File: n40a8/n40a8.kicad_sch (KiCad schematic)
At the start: 93 parts, among them J1 Conn_01x16, SW1 SW_Push, SW10 SW_Push, SW11 SW_Push, SW12 SW_Push, SW13 SW_Push, SW14 SW_Push, SW15 SW_Push, SW16 SW_Push, SW17 SW_Push, SW18 SW_Push, SW19 SW_Push, SW2 SW_Push, SW20 SW_Push, SW21 SW_Push, SW22 SW_Push, SW23 SW_Push, SW24 SW_Push, SW25 SW_Push, SW26 SW_Push, SW27 SW_Push, SW28 SW_Push, SW29 SW_Push, SW3 SW_Push, SW30 SW_Push, SW31 SW_Push, SW32 SW_Push, SW33 SW_Push, SW34 SW_Push, SW35 SW_Push, SW36 SW_Push, SW37 SW_Push, SW38 SW_Push, SW39 SW_Push, SW4 SW_Push, SW40 SW_Push, SW41 SW_Push, SW42 SW_Push, SW43 SW_RST, SW44 SW_PWR, SW5 SW_Push, SW6 SW_Push, SW7 SW_Push, SW8 SW_Push, SW9 SW_Push, U1 BLE-Micro-Pro-2, U2 TPS61221

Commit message: move Diode
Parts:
- SW38: footprint cscslib:CPG151101S11_2u_RS -> cscslib:CPG151101S11_2u
- SW39: footprint cscslib:CPG151101S11_1.25u -> cscslib:CPG151101S11_2.25u
- SW40: footprint cscslib:CPG151101S11_2.25u_RS -> cscslib:CPG151101S11_1.25u
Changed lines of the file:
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@@
 			)
 		)
-		(property "Footprint" "cscslib:CPG151101S11_1.25u"
+		(property "Footprint" "cscslib:CPG151101S11_2.25u"
 			(at 137.16 115.57 0)
 			(effects
@@
 			)
 		)
-		(property "Footprint" "cscslib:CPG151101S11_2u_RS"
+		(property "Footprint" "cscslib:CPG151101S11_2u"
 			(at 83.82 115.57 0)
 			(effects
@@
 			)
 		)
-		(property "Footprint" "cscslib:CPG151101S11_2.25u_RS"
+		(property "Footprint" "cscslib:CPG151101S11_1.25u"
 			(at 154.94 115.57 0)
 			(effects

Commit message: wired
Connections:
- net C2: no longer SW37.1
- net C3: now also SW37.1; no longer SW38.1
- net C4: now also SW38.1
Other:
- moved on the sheet: D37, D38, SW37, SW38
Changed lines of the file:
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@@
 	)
 	(junction
-		(at 71.12 128.27)
-		(diameter 0)
-		(color 0 0 0 0)
-	)
-	(junction
 		(at 185.42 87.63)
 		(diameter 0)
@@
 	)
 	(junction
-		(at 78.74 104.14)
+		(at 96.52 71.12)
 		(diameter 0)
 		(color 0 0 0 0)
 	)
 	(junction
-		(at 96.52 71.12)
+		(at 106.68 128.27)
 		(diameter 0)
 		(color 0 0 0 0)
@@
 	)
 	(junction
+		(at 88.9 128.27)
+		(diameter 0)
+		(color 0 0 0 0)
+	)
+	(junction
 		(at 167.64 71.12)
 		(diameter 0)
@@
 	)
 	(junction
+		(at 78.74 104.14)
+		(diameter 0)
+		(color 0 0 0 0)
+	)
+	(junction
 		(at 29.21 176.53)
 		(diameter 0)
@@
 	)
 	(junction
-		(at 88.9 128.27)
-		(diameter 0)
-		(color 0 0 0 0)
-	)
-	(junction
 		(at 35.56 78.74)
 		(diameter 0)
@@
 	)
 	(junction
-		(at 60.96 104.14)
+		(at 160.02 95.25)
 		(diameter 0)
 		(color 0 0 0 0)
 	)
 	(junction
-		(at 160.02 95.25)
+		(at 96.52 104.14)
 		(diameter 0)
 		(color 0 0 0 0)
@@
 	(wire
 		(pts
-			(xy 203.2 71.12) (xy 203.2 87.63)
+			(xy 106.68 128.27) (xy 142.24 128.27)
 		)
 		(stroke
@@
 	(wire
 		(pts
-			(xy 60.96 48.26) (xy 66.04 48.26)
+			(xy 203.2 71.12) (xy 203.2 87.63)
 		)
 		(stroke
@@
 	(wire
 		(pts
-			(xy 177.8 111.76) (xy 195.58 111.76)
+			(xy 60.96 48.26) (xy 66.04 48.26)
 		)
 		(stroke
@@
 	(wire
 		(pts
-			(xy 40.64 167.64) (xy 62.23 167.64)
+			(xy 177.8 111.76) (xy 195.58 111.76)
 		)
 		(stroke
@@
 	(wire
 		(pts
-			(xy 269.24 55.88) (xy 269.24 54.61)
+			(xy 40.64 167.64) (xy 62.23 167.64)
 		)
 		(stroke
@@
 	(wire
 		(pts
-			(xy 106.68 78.74) (xy 124.46 78.74)
+			(xy 269.24 55.88) (xy 269.24 54.61)
 		)
 		(stroke
@@
 	(wire
 		(pts
-			(xy 63.5 181.61) (xy 63.5 182.88)
+			(xy 106.68 78.74) (xy 124.46 78.74)
 		)
 		(stroke
@@
 	(wire
 		(pts
-			(xy 231.14 78.74) (xy 241.3 78.74)
+			(xy 63.5 181.61) (xy 63.5 182.88)
 		)
 		(stroke
@@
 	(wire
 		(pts
-			(xy 60.96 104.14) (xy 60.96 120.65)
+			(xy 231.14 78.74) (xy 241.3 78.74)
 		)
 		(stroke
@@
 	(wire
 		(pts
-			(xy 53.34 128.27) (xy 71.12 128.27)
+			(xy 53.34 128.27) (xy 88.9 128.27)
 		)
 		(stroke
@@
 	(wire
 		(pts
-			(xy 149.86 71.12) (xy 149.86 87.63)
+			(xy 78.74 104.14) (xy 78.74 120.65)
 		)
 		(stroke
@@
 	(wire
 		(pts
-			(xy 88.9 95.25) (xy 106.68 95.25)
+			(xy 149.86 71.12) (xy 149.86 87.63)
 		)
 		(stroke
@@
 	(wire
 		(pts
-			(xy 71.12 128.27) (xy 88.9 128.27)
+			(xy 88.9 95.25) (xy 106.68 95.25)
 		)
 		(stroke
@@
 	(wire
 		(pts
+			(xy 88.9 128.27) (xy 106.68 128.27)
+		)
+		(stroke
+			(width 0)
+			(type default)
+		)
+	)
+	(wire
+		(pts
 			(xy 177.8 78.74) (xy 195.58 78.74)
 		)
@@
 	(wire
 		(pts
-			(xy 88.9 128.27) (xy 142.24 128.27)
-		)
-		(stroke
-			(width 0)
-			(type default)
-		)
-	)
-	(wire
-		(pts
 			(xy 38.1 189.23) (xy 38.1 190.5)
 		)
@@
 	(wire
 		(pts
+			(xy 96.52 104.14) (xy 96.52 120.65)
+		)
+		(stroke
+			(width 0)
+			(type default)
+		)
+	)
+	(wire
+		(pts
 			(xy 60.96 50.8) (xy 66.04 50.8)
 		)
@@
 	(wire
 		(pts
-			(xy 78.74 104.14) (xy 78.74 120.65)
-		)
-		(stroke
-			(width 0)
-			(type default)
-		)
-	)
-	(wire
-		(pts
 			(xy 78.74 63.5) (xy 78.74 71.12)
 		)
@@
 	(symbol
 		(lib_id "Switch:SW_Push")
-		(at 83.82 120.65 0)
+		(at 101.6 120.65 0)
 		(unit 1)
 		(exclude_from_sim no)
@@
 		(dnp no)
 		(property "Reference" "SW38"
-			(at 83.82 113.411 0)
+			(at 101.6 113.411 0)
 			(effects
 				(font
@@
 		)
 		(property "Value" "SW_Push"
-			(at 83.82 115.7224 0)
+			(at 101.6 115.7224 0)
 			(effects
 				(font
@@
 		)
 		(property "Footprint" "cscslib:CPG151101S11_2u"
-			(at 83.82 115.57 0)
+			(at 101.6 115.57 0)
 			(effects
 				(font
@@
 		)
 		(property "Datasheet" ""
-			(at 83.82 115.57 0)
+			(at 101.6 115.57 0)
 			(effects
 				(font
@@
 		)
 		(property "Description" ""
-			(at 83.82 120.65 0)
+			(at 101.6 120.65 0)
 			(effects
 				(font
@@
 	(symbol
 		(lib_id "Switch:SW_Push")
-		(at 66.04 120.65 0)
+		(at 83.82 120.65 0)
 		(unit 1)
 		(exclude_from_sim no)
@@
 		(dnp no)
 		(property "Reference" "SW37"
-			(at 66.04 113.411 0)
+			(at 83.82 113.411 0)
 			(effects
 				(font
@@
 		)
 		(property "Value" "SW_Push"
-			(at 66.04 115.7224 0)
+			(at 83.82 115.7224 0)
 			(effects
 				(font
@@
 		)
 		(property "Footprint" "cscslib:CPG151101S11_1.25u"
-			(at 66.04 115.57 0)
+			(at 83.82 115.57 0)
 			(effects
 				(font
@@
 		)
 		(property "Datasheet" ""
-			(at 66.04 115.57 0)
+			(at 83.82 115.57 0)
 			(effects
 				(font
@@
 		)
 		(property "Description" ""
-			(at 66.04 120.65 0)
+			(at 83.82 120.65 0)
 			(effects
 				(font
@@
 	(symbol
 		(lib_id "Diode:1N4148W")
-		(at 88.9 124.46 90)
+		(at 106.68 124.46 90)
 		(unit 1)
 		(exclude_from_sim no)
@@
 		(dnp no)
 		(property "Reference" "D38"
-			(at 90.6272 123.2916 90)
+			(at 108.4072 123.2916 90)
 			(effects
 				(font
@@
 		)
 		(property "Value" "D"
-			(at 90.6272 125.603 90)
+			(at 108.4072 125.603 90)
 			(effects
 				(font
@@
 		)
 		(property "Footprint" "Diode_SMD:D_SOD-123"
-			(at 93.345 124.46 0)
+			(at 111.125 124.46 0)
 			(effects
 				(font
@@
 		)
 		(property "Datasheet" "https://www.vishay.com/docs/85748/1n4148w.pdf"
-			(at 88.9 124.46 0)
+			(at 106.68 124.46 0)
 			(effects
 				(font
@@
 		)
 		(property "Description" "75V 0.15A Fast Switching Diode, SOD-123"
-			(at 88.9 124.46 0)
+			(at 106.68 124.46 0)
 			(effects
 				(font
@@
 		)
 		(property "Sim.Device" "D"
-			(at 88.9 124.46 0)
+			(at 106.68 124.46 0)
 			(effects
 				(font
@@
 		)
 		(property "Sim.Pins" "1=K 2=A"
-			(at 88.9 124.46 0)
+			(at 106.68 124.46 0)
 			(effects
 				(font
@@
 	(symbol
 		(lib_id "Diode:1N4148W")
-		(at 71.12 124.46 90)
+		(at 88.9 124.46 90)
 		(unit 1)
 		(exclude_from_sim no)
@@
 		(dnp no)
 		(property "Reference" "D37"
-			(at 72.8472 123.2916 90)
+			(at 90.6272 123.2916 90)
 			(effects
 				(font
@@
 		)
 		(property "Value" "D"
-			(at 72.8472 125.603 90)
+			(at 90.6272 125.603 90)
 			(effects
 				(font
@@
 		)
 		(property "Footprint" "Diode_SMD:D_SOD-123"
-			(at 75.565 124.46 0)
+			(at 93.345 124.46 0)
 			(effects
 				(font
@@
 		)
 		(property "Datasheet" "https://www.vishay.com/docs/85748/1n4148w.pdf"
-			(at 71.12 124.46 0)
+			(at 88.9 124.46 0)
 			(effects
 				(font
@@
 		)
 		(property "Description" "75V 0.15A Fast Switching Diode, SOD-123"
-			(at 71.12 124.46 0)
+			(at 88.9 124.46 0)
 			(effects
 				(font
@@
 		)
 		(property "Sim.Device" "D"
-			(at 71.12 124.46 0)
+			(at 88.9 124.46 0)
 			(effects
 				(font
@@
 		)
 		(property "Sim.Pins" "1=K 2=A"
-			(at 71.12 124.46 0)
+			(at 88.9 124.46 0)
 			(effects
 				(font

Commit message: wiring complete
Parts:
- removed J1: Conn_01x16, cscslib:PinHeader_1x16_P1.27mm_Conthrough, symbol Connector_Generic:Conn_01x16
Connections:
- net C0: now also U1.14 (PB2); no longer U1.12 (PB5)
- net C1: now also U1.15 (PB3); no longer U1.11 (PB4)
- net C10: now also U1.5 (SCL); no longer U1.18 (PF6)
- net C2: now also U1.16 (PB1); no longer U1.10 (PE6)
- net C3: now also U1.17 (PF7); no longer U1.9 (PD7)
- net C4: now also U1.18 (PF6); no longer U1.8 (PC6)
- net C5: now also U1.19 (PF5); no longer U1.7 (PD4)
- net C6: now also U1.20 (PF4); no longer U1.6 (SDA)
- net C7: now also U1.8 (PC6); no longer U1.5 (SCL)
- net C8: now also U1.7 (PD4); no longer U1.20 (PF4)
- net C9: now also U1.6 (SDA); no longer U1.19 (PF5)
- net R0: now also U1.12 (PB5); no longer U1.17 (PF7)
- net R1: now also U1.11 (PB4); no longer U1.16 (PB1)
- net R2: now also U1.10 (PE6); no longer U1.15 (PB3)
- net R3: now also U1.9 (PD7); no longer U1.14 (PB2)

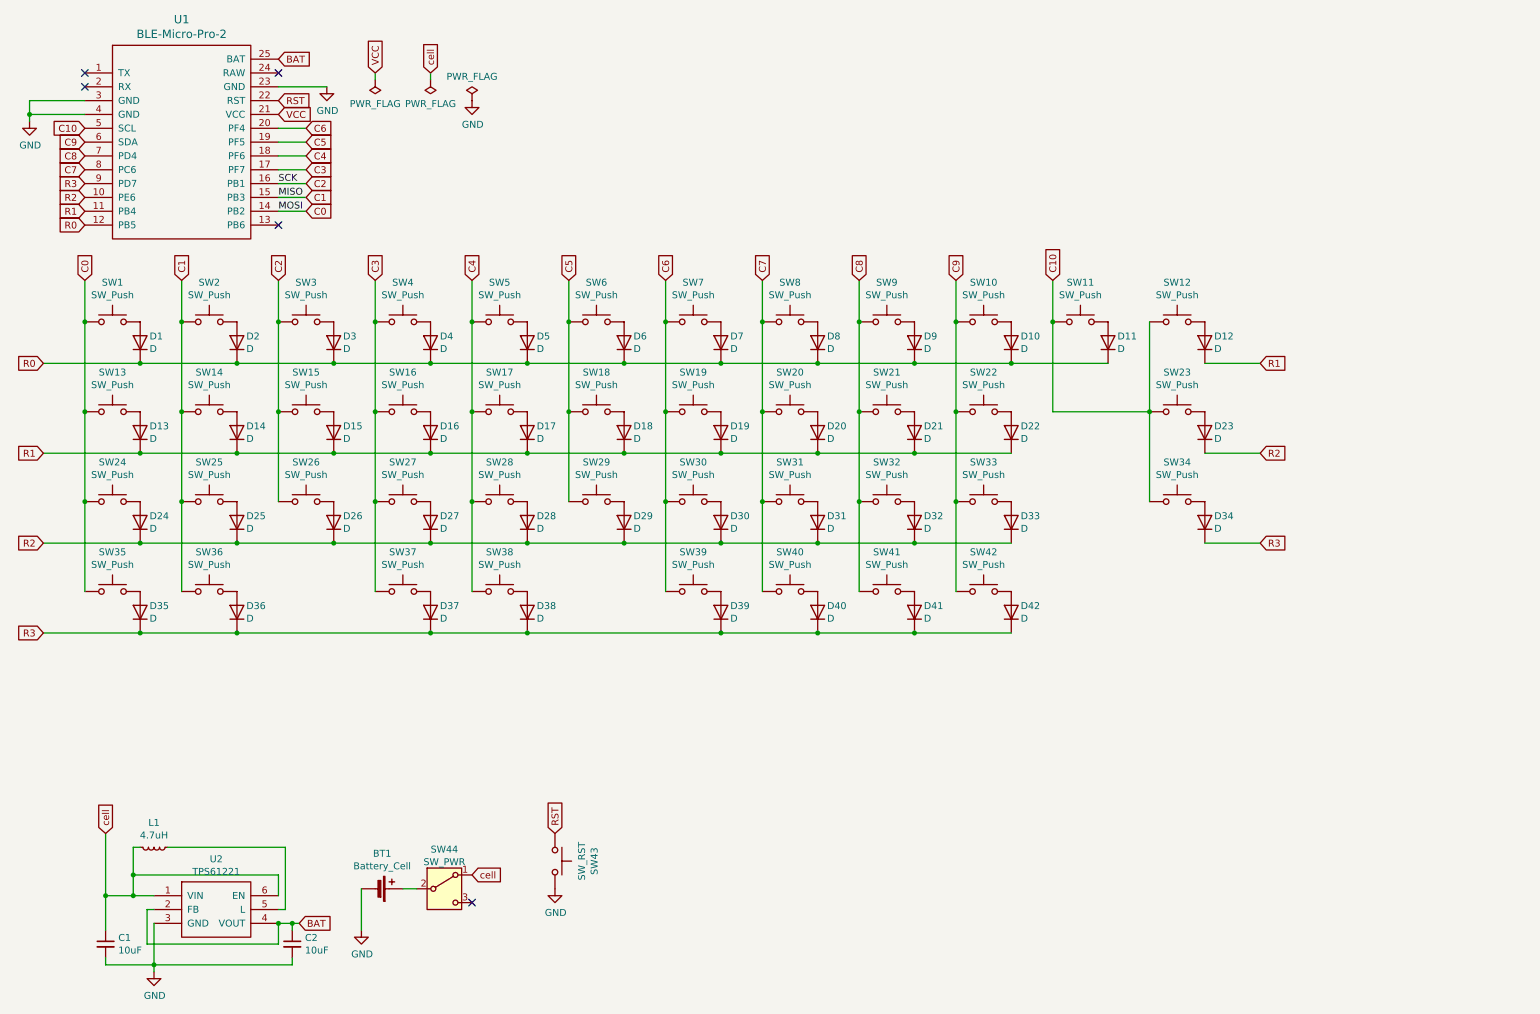
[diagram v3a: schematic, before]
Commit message: revise foot print for PCBA
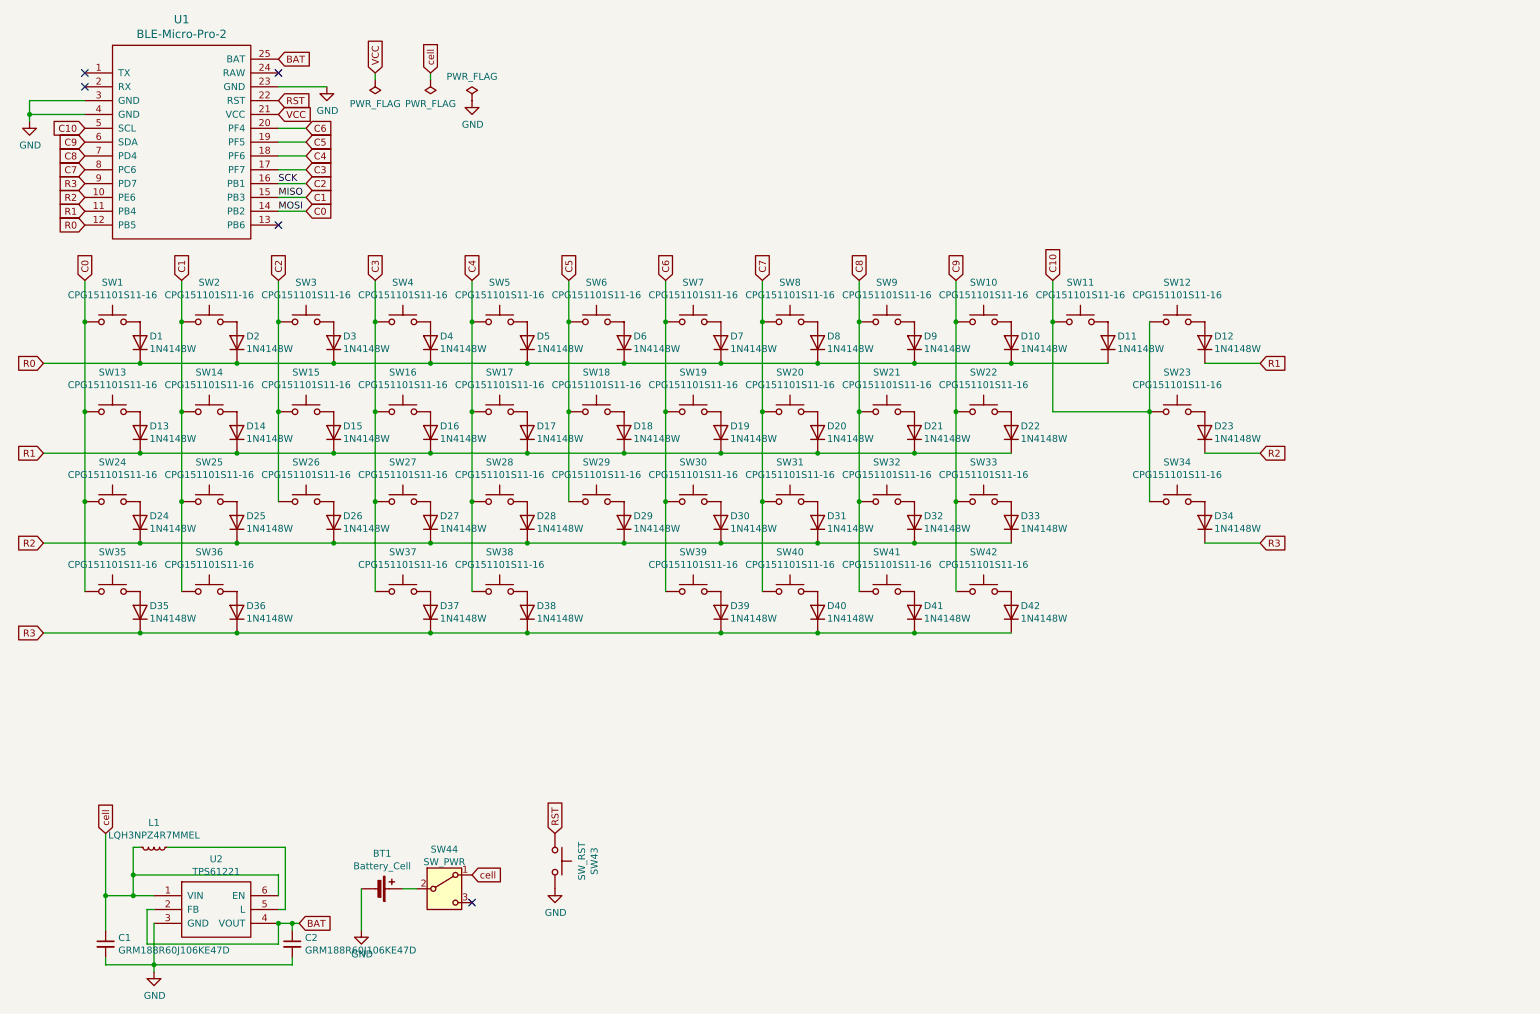
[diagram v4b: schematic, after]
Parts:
- C1, C2: value 10uF -> GRM188R60J106KE47D
- D1, D10, D11, D12, D13, D14, D15, D16, D17, D18, D19, D2, D20, D21, D22, D23, D24, D25, D26, D27, D28, D29, D3, D30, D31, D32, D33, D34, D35, D36, D37, D38, D39, D4, D40, D41, D42, D5, D6, D7, D8, D9: value D -> 1N4148W
- L1: value 4.7uH -> LQH3NPZ4R7MMEL
- SW1, SW10, SW11, SW12, SW13, SW14, SW15, SW16, SW17, SW18, SW19, SW2, SW20, SW21, SW22, SW23, SW24, SW25, SW26, SW27, SW28, SW29, SW3, SW30, SW31, SW32, SW33, SW34, SW35, SW36, SW37, SW38, SW39, SW4, SW40, SW41, SW42, SW5, SW6, SW7, SW8, SW9: value SW_Push -> CPG151101S11-16

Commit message: revice for PCBA
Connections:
- net C10: now also U1.20 (PF4); no longer U1.5 (SCL)
- net C6: now also U1.8 (PC6); no longer U1.20 (PF4)
- net C7: now also U1.7 (PD4); no longer U1.8 (PC6)
- net C8: now also U1.6 (SDA); no longer U1.7 (PD4)
- net C9: now also U1.5 (SCL); no longer U1.6 (SDA)
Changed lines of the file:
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@@
 	(global_label "C9"
 		(shape input)
-		(at 25.4 38.1 180)
-		(effects
-			(font
-				(size 1.27 1.27)
-			)
-			(justify right)
-		)
-		(property "Intersheetrefs" "${INTERSHEET_REFS}"
-			(at 25.4 38.1 0)
+		(at 25.4 35.56 180)
+		(effects
+			(font
+				(size 1.27 1.27)
+			)
+			(justify right)
+		)
+		(property "Intersheetrefs" "${INTERSHEET_REFS}"
+			(at 25.4 35.56 0)
 			(effects
 				(font
@@
 	(global_label "C7"
 		(shape input)
+		(at 25.4 40.64 180)
+		(effects
+			(font
+				(size 1.27 1.27)
+			)
+			(justify right)
+		)
+		(property "Intersheetrefs" "${INTERSHEET_REFS}"
+			(at 25.4 40.64 0)
+			(effects
+				(font
+					(size 1.27 1.27)
+				)
+				(hide yes)
+			)
+		)
+	)
+	(global_label "BAT"
+		(shape input)
+		(at 60.96 22.86 0)
+		(effects
+			(font
+				(size 1.27 1.27)
+			)
+			(justify left)
+		)
+		(property "Intersheetrefs" "${INTERSHEET_REFS}"
+			(at 60.96 22.86 0)
+			(effects
+				(font
+					(size 1.27 1.27)
+				)
+				(hide yes)
+			)
+		)
+	)
+	(global_label "VCC"
+		(shape input)
+		(at 78.74 25.4 90)
+		(effects
+			(font
+				(size 1.27 1.27)
+			)
+			(justify left)
+		)
+		(property "Intersheetrefs" "${INTERSHEET_REFS}"
+			(at 78.74 25.4 0)
+			(effects
+				(font
+					(size 1.27 1.27)
+				)
+				(hide yes)
+			)
+		)
+	)
+	(global_label "C10"
+		(shape input)
+		(at 203.2 63.5 90)
+		(effects
+			(font
+				(size 1.27 1.27)
+			)
+			(justify left)
+		)
+		(property "Intersheetrefs" "${INTERSHEET_REFS}"
+			(at 203.2 63.5 0)
+			(effects
+				(font
+					(size 1.27 1.27)
+				)
+				(hide yes)
+			)
+		)
+	)
+	(global_label "C6"
+		(shape input)
 		(at 25.4 43.18 180)
 		(effects
@@
 		)
 	)
-	(global_label "BAT"
-		(shape input)
-		(at 60.96 22.86 0)
-		(effects
-			(font
-				(size 1.27 1.27)
-			)
-			(justify left)
-		)
-		(property "Intersheetrefs" "${INTERSHEET_REFS}"
-			(at 60.96 22.86 0)
-			(effects
-				(font
-					(size 1.27 1.27)
-				)
-				(hide yes)
-			)
-		)
-	)
-	(global_label "VCC"
-		(shape input)
-		(at 78.74 25.4 90)
-		(effects
-			(font
-				(size 1.27 1.27)
-			)
-			(justify left)
-		)
-		(property "Intersheetrefs" "${INTERSHEET_REFS}"
-			(at 78.74 25.4 0)
+	(global_label "C0"
+		(shape input)
+		(at 66.04 50.8 0)
+		(effects
+			(font
+				(size 1.27 1.27)
+			)
+			(justify left)
+		)
+		(property "Intersheetrefs" "${INTERSHEET_REFS}"
+			(at 66.04 50.8 0)
+			(effects
+				(font
+					(size 1.27 1.27)
+				)
+				(hide yes)
+			)
+		)
+	)
+	(global_label "C5"
+		(shape input)
+		(at 66.04 38.1 0)
+		(effects
+			(font
+				(size 1.27 1.27)
+			)
+			(justify left)
+		)
+		(property "Intersheetrefs" "${INTERSHEET_REFS}"
+			(at 66.04 38.1 0)
+			(effects
+				(font
+					(size 1.27 1.27)
+				)
+				(hide yes)
+			)
+		)
+	)
+	(global_label "cell"
+		(shape input)
+		(at 96.52 172.72 0)
+		(effects
+			(font
+				(size 1.27 1.27)
+			)
+			(justify left)
+		)
+		(property "Intersheetrefs" "${INTERSHEET_REFS}"
+			(at 96.52 172.72 0)
+			(effects
+				(font
+					(size 1.27 1.27)
+				)
+				(hide yes)
+			)
+		)
+	)
+	(global_label "C2"
+		(shape input)
+		(at 66.04 45.72 0)
+		(effects
+			(font
+				(size 1.27 1.27)
+			)
+			(justify left)
+		)
+		(property "Intersheetrefs" "${INTERSHEET_REFS}"
+			(at 66.04 45.72 0)
+			(effects
+				(font
+					(size 1.27 1.27)
+				)
+				(hide yes)
+			)
+		)
+	)
+	(global_label "C5"
+		(shape input)
+		(at 114.3 63.5 90)
+		(effects
+			(font
+				(size 1.27 1.27)
+			)
+			(justify left)
+		)
+		(property "Intersheetrefs" "${INTERSHEET_REFS}"
+			(at 114.3 63.5 0)
+			(effects
+				(font
+					(size 1.27 1.27)
+				)
+				(hide yes)
+			)
+		)
+	)
+	(global_label "C8"
+		(shape input)
+		(at 25.4 38.1 180)
+		(effects
+			(font
+				(size 1.27 1.27)
+			)
+			(justify right)
+		)
+		(property "Intersheetrefs" "${INTERSHEET_REFS}"
+			(at 25.4 38.1 0)
 			(effects
 				(font
@@
 	(global_label "C10"
 		(shape input)
-		(at 203.2 63.5 90)
-		(effects
-			(font
-				(size 1.27 1.27)
-			)
-			(justify left)
-		)
-		(property "Intersheetrefs" "${INTERSHEET_REFS}"
-			(at 203.2 63.5 0)
-			(effects
-				(font
-					(size 1.27 1.27)
-				)
-				(hide yes)
-			)
-		)
-	)
-	(global_label "C6"
-		(shape input)
 		(at 66.04 35.56 0)
 		(effects
@@
 			(effects
 				(font
-					(size 1.27 1.27)
-				)
-				(hide yes)
-			)
-		)
-	)
-	(global_label "C0"
-		(shape input)
-		(at 66.04 50.8 0)
-		(effects
-			(font
-				(size 1.27 1.27)
-			)
-			(justify left)
-		)
-		(property "Intersheetrefs" "${INTERSHEET_REFS}"
-			(at 66.04 50.8 0)
-			(effects
-				(font
-					(size 1.27 1.27)
-				)
-				(hide yes)
-			)
-		)
-	)
-	(global_label "C5"
-		(shape input)
-		(at 66.04 38.1 0)
-		(effects
-			(font
-				(size 1.27 1.27)
-			)
-			(justify left)
-		)
-		(property "Intersheetrefs" "${INTERSHEET_REFS}"
-			(at 66.04 38.1 0)
-			(effects
-				(font
-					(size 1.27 1.27)
-				)
-				(hide yes)
-			)
-		)
-	)
-	(global_label "cell"
-		(shape input)
-		(at 96.52 172.72 0)
-		(effects
-			(font
-				(size 1.27 1.27)
-			)
-			(justify left)
-		)
-		(property "Intersheetrefs" "${INTERSHEET_REFS}"
-			(at 96.52 172.72 0)
-			(effects
-				(font
-					(size 1.27 1.27)
-				)
-				(hide yes)
-			)
-		)
-	)
-	(global_label "C2"
-		(shape input)
-		(at 66.04 45.72 0)
-		(effects
-			(font
-				(size 1.27 1.27)
-			)
-			(justify left)
-		)
-		(property "Intersheetrefs" "${INTERSHEET_REFS}"
-			(at 66.04 45.72 0)
-			(effects
-				(font
-					(size 1.27 1.27)
-				)
-				(hide yes)
-			)
-		)
-	)
-	(global_label "C5"
-		(shape input)
-		(at 114.3 63.5 90)
-		(effects
-			(font
-				(size 1.27 1.27)
-			)
-			(justify left)
-		)
-		(property "Intersheetrefs" "${INTERSHEET_REFS}"
-			(at 114.3 63.5 0)
-			(effects
-				(font
-					(size 1.27 1.27)
-				)
-				(hide yes)
-			)
-		)
-	)
-	(global_label "C8"
-		(shape input)
-		(at 25.4 40.64 180)
-		(effects
-			(font
-				(size 1.27 1.27)
-			)
-			(justify right)
-		)
-		(property "Intersheetrefs" "${INTERSHEET_REFS}"
-			(at 25.4 40.64 0)
-			(effects
-				(font
-					(size 1.27 1.27)
-				)
-				(hide yes)
-			)
-		)
-	)
-	(global_label "C10"
-		(shape input)
-		(at 25.4 35.56 180)
-		(effects
-			(font
-				(size 1.27 1.27)
-			)
-			(justify right)
-		)
-		(property "Intersheetrefs" "${INTERSHEET_REFS}"
-			(at 25.4 35.56 0)
-			(effects
-				(font
